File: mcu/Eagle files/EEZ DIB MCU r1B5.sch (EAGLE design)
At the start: 193 parts, among them IC1 TPD4E001DRLR, IC10 TPS61169DCKR, IC11 TPD4E001DRLR, IC12 TPA6205A1DGN, IC13 TPD4E001DRLR, IC14 TSC2007IPW, IC15 TPD4E001DRLR, IC16 DP83848CVV/NOPB, IC2 SN74LVC2G34DBVR, IC3 BTS3408G, IC4 STM32F769IGT6, IC5 LD1117ADT33TR, IC6 TPD4E001DRLR, IC7 IS42S16400J, IC8 AT24C256C-SSHL-B, IC9 TPS2051BDBVR, J1 503398-1892, J2 67803-8020, Q1 MMBT5551, SW1 TL1100CF160Q, SW2 PEC16-2215F-S0024, X1 ZL263-40DG, X2 ZL231-16KG, X3 1844249, X4 22-23-2061, X5 LMJTAB881243M-L, Y1 25MHz, Y2 XTAL016178-85SMX

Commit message: #44, #45 Eagle files
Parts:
- removed C67: 10u, EEZ_Lib1:ECAP1206
- removed C68, C69, C70, C71: 100n, rcl:C-EUC0603
- removed F1, F2: 50mA, EEZ_Lib1:FUSE_RESETTABLE21210
- removed IC14: TSC2007IPW, EEZ_Lib1:TSC2007IPW
- removed IC15: TPD4E001DRLR, EEZ_Lib1:TPD4E001-DRL
- removed IC16: DP83848CVV/NOPB, EEZ_Lib1:DP83848CVV/NOPB
- removed R50, R53, R54, R56: 2K2, rcl:R-EU_R0805
- removed R51, R52: 220R, rcl:R-EU_R0805
- removed R55: 4K87, rcl:R-EU_R0805
- removed ZD2: SMAJ18A, EEZ_Lib1:PSMAXX
- removed ZD3: BZX384-B30.115, EEZ_Lib1:ZENER-DIODESOD323
- added Q2: 2N7002, EEZ_Lib1:2N7002
- C11: value 18p -> EEEFK1V470P; device rcl:C-EUC0603 -> EEZ_Lib1:ECAPPANASONIC_H
- C12: value 4p7 -> 100n
- C13: value EEEFK1V470P -> 4u7; device EEZ_Lib1:ECAPPANASONIC_H -> EEZ_Lib1:ECAP1206
- C15: value 4u7 -> 100n; device EEZ_Lib1:ECAP1206 -> rcl:C-EUC0603
- C2, C5: value 100n -> 10n; device rcl:C-EUC0603 -> rcl:C-EUC0805
- C20: value 100n -> 4u7; device rcl:C-EUC0603 -> EEZ_Lib1:ECAP1206
- C22: value 4u7 -> 1u; device EEZ_Lib1:ECAP1206 -> rcl:C-EUC0805
- C23, C52: value 100n -> N.C.
- C24, C33, C58: value 1u -> 100n; device rcl:C-EUC0805 -> rcl:C-EUC0603
- C25: value N.C. -> 100n
- C31, C32, C46: value 100n -> 1u; device rcl:C-EUC0603 -> rcl:C-EUC0805
- C34, C48: value 1u -> 2u2
- C35: value 100n -> 2u2; device rcl:C-EUC0603 -> rcl:C-EUC0805
- C36: value 2u2 -> N.C.; device rcl:C-EUC0805 -> rcl:C-EUC0603
- C37: value 2u2 -> 4u7; device rcl:C-EUC0805 -> rcl:C-EUC1206
- C39, C53: value 4u7 -> 100n; device rcl:C-EUC1206 -> rcl:C-EUC0603
- C4: value 10n -> 100n; device rcl:C-EUC0805 -> rcl:C-EUC0603
- C45: value 100n -> 4u7; device rcl:C-EUC0603 -> rcl:C-EUC1206
- C47: device rcl:C-EUC1206 -> EEZ_Lib1:ECAP1206
- C49: value 4u7 -> N.C.; device EEZ_Lib1:ECAP1206 -> rcl:C-EUC1210
- C50: value 2u2 -> 100n; device rcl:C-EUC0805 -> rcl:C-EUC0603
- C51: value N.C. -> 4u7; device rcl:C-EUC1210 -> rcl:C-EUC1206
- C54: value 470n -> 1u
- C55: value 470n -> N.C.; device rcl:C-EUC0805 -> rcl:C-EUC0603
- C59: value N.C. -> 100n; device rcl:C-EUC0805 -> rcl:C-EUC0603
- C62: value 100n -> 10u; device rcl:C-EUC0603 -> EEZ_Lib1:ECAP1206
- C7: value 10n -> 18p; device rcl:C-EUC0805 -> rcl:C-EUC0603
- C8: value 100n -> 4p7
- IC1: value TPD4E001DRLR -> CD74HC4050PWR; device EEZ_Lib1:TPD4E001-DRL -> EEZ_DIB:CD74HC4050PWR
- IC10: value TPS61169DCKR -> TPD4E001DRLR; device EEZ_Lib1:TPS61169DCKR -> EEZ_Lib1:TPD4E001-DRL
- IC11: value TPD4E001DRLR -> TSC2007IPW; device EEZ_Lib1:TPD4E001-DRL -> EEZ_Lib1:TSC2007IPW
- IC12: value TPA6205A1DGN -> TPD4E001DRLR; device EEZ_Lib1:TPA6205 -> EEZ_Lib1:TPD4E001-DRL
- IC13: value TPD4E001DRLR -> DP83848CVV/NOPB; device EEZ_Lib1:TPD4E001-DRL -> EEZ_Lib1:DP83848CVV/NOPB
- IC2: value SN74LVC2G34DBVR -> STM32F769IGT6; device EEZ_Lib1:SN74LVC2G34DBVR -> EEZ_DIB:STM32F769IXT
- IC3: value BTS3408G -> LD1117ADT33TR; device EEZ_Lib1:BTS3408G -> v-reg:LD117ADT33TR
- IC4: value STM32F769IGT6 -> TPD4E001DRLR; device EEZ_DIB:STM32F769IXT -> EEZ_Lib1:TPD4E001-DRL
- IC5: value LD1117ADT33TR -> IS42S16400J; device v-reg:LD117ADT33TR -> EEZ_Lib1:IS42S16400
- IC6: value TPD4E001DRLR -> AT24C256C-SSHL-B; device EEZ_Lib1:TPD4E001-DRL -> EEZ_Lib1:AT24CXXSOIC8
- IC7: value IS42S16400J -> TPS2051BDBVR; device EEZ_Lib1:IS42S16400 -> EEZ_Lib1:TPS2051B
- IC8: value AT24C256C-SSHL-B -> TPS61169DCKR; device EEZ_Lib1:AT24CXXSOIC8 -> EEZ_Lib1:TPS61169DCKR
- IC9: value TPS2051BDBVR -> TPD4E001DRLR; device EEZ_Lib1:TPS2051B -> EEZ_Lib1:TPD4E001-DRL
- Q1: value MMBT5551 -> N.C.
- R18: value 10K -> N.C.
- R19, R20: value 22R -> N.C.
- R2: value 4K7 -> 10K
- R25: value 330R -> N.C.
- R28: value 47K -> N.C.
- R32: value 10K -> 1K5
- R33, R34, R37: value 10K -> 49R9
- R35, R38: value 10K -> 2K2
- R36: value 47K -> 2K2
- R39: value 1K5 -> N.C.
- R4, R8: value 1K -> 4K7
- R40, R41, R49: value 49R9 -> 2K2
- R42: value 2K2 -> 49R9
- R44: value 49R9 -> 220R
- R45: value 2K2 -> 220R
- R46: value 220R -> 2K2
- R48: value 2K2 -> 4K87
- R5: value 10K -> 1K
- R9: value 4K7 -> 1K
- SP1: value LD-BZEL-M1313 -> AI-1223-TWT or LD-BZEN 0903; device EEZ_Lib1:LD-BZEL-M1313 -> EEZ_Lib1:AI-1223-TWT-LDB0903
- SPEED: value LTST-C170YKT -> N.C.
- VBUS: value HSMG-C170 -> N.C.
- X4: value 22-23-2061 -> N.C.
- ZD1: value SMAJ18A -> BZX384-B30.115; device EEZ_Lib1:PSMAXX -> EEZ_Lib1:ZENER-DIODESOD323
- renumbered BOOT0 to BOOT1
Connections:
- removed net !AUDIO_SHDN: IC12.!SHDN, R36.1
- removed net N$166: IC12.VO-, R33.1, SP1.-
- removed net N$171: IC12.IN-, R35.1, R37.2
- removed net N$181: IC12.IN+, R32.2, R34.1
- removed net N$193: C54.1, R34.2
- removed net N$194: C59.2, IC12.BYPASS
- removed net N$195: C55.1, R35.2
- removed net N$44: F1.P$1, X3-4.1
- removed net N$45: F2.P$1, X3-5.1
- removed net N$50: IC12.VO+, R38.1, SP1.+
- removed net N$6: R37.1, R38.2
- net !FAULT: now also IC2A.PB2; no longer IC3.!FAULT, IC4A.PB2
- net !RESET: now also IC13.RESET_N, IC2C.NRST, IC4.IO3; no longer IC16.RESET_N, IC3.ENA, IC4C.NRST, IC6.IO3
- net !USB_OTG_FS_OC: now also IC2A.PD4, IC7.!OC; no longer IC4A.PD4, IC9.!OC
- net +3V3: now also C13.+, C36.1, C37.1, C38.2, C4.1, C40.1, C48.1, C52.2, C53.2, C54.2, C55.1, C65.1, C66.1, IC10.VCC, IC11.VDD/REF, IC12.VCC, IC13.IOVDD33-32, IC13.IOVDD33-48, IC1P.VDD, IC3.OUT, IC4.VCC, IC5.VDD-1, IC5.VDD-14, IC5.VDD-27, IC5.VDDQ-3, IC5.VDDQ-43, IC5.VDDQ-49, IC5.VDDQ-9, R32.2, R36.1, R39.1, R40.1, R41.1, R49.1, R6.1; no longer C15.+, C38.1, C40.2, C45.1, C46.1, C5.1, C50.1, C56.2, C57.2, C58.2, C60.1, C70.1, C71.1, IC13.VCC, IC14.VDD/REF, IC15.VCC, IC16.IOVDD33-32, IC16.IOVDD33-48, IC2P.VDD, IC5.OUT, IC7.VDD-1, IC7.VDD-14, IC7.VDD-27, IC7.VDDQ-3, IC7.VDDQ-43, IC7.VDDQ-49, IC7.VDDQ-9, IC8.VCC, R36.2, R39.2, R48.1, R50.1, R53.1, R54.1, R56.1, R9.1
- net +3V3(A): now also C57.2, C59.2, C64.1, IC13.AVDD33; no longer C62.2, C64.2, C69.1, IC16.AVDD33
- net +5V: now also C11.+, C12.1, C45.1, IC3.IN, IC7.IN; no longer C13.+, C14.1, C2.1, C47.1, C8.2, IC1.VCC, IC3.VSS, IC5.IN, IC9.IN
- net BOOT0: now also IC2C.BOOT0; no longer IC4C.BOOT0
- net BYPASS_REG: now also IC2C.BYPASS_REG; no longer IC4C.BYPASS_REG
- net DAC_OUT1: now also IC2A.PA4, Q2.G; no longer C55.2, IC4A.PA4
- net DIN2: now also IC2A.PC13, R9.2; no longer IC4A.PC13, R8.2
- net DOUT2: now also IC1C.I, IC1D.I, IC2A.PB5; no longer IC3.IN2, IC4A.PB5
- net ENC_A: now also C5.2, IC2A.PC6, R2.1; no longer C6.2, IC4A.PC6, R5.1
- net ENC_B: now also C6.1, IC2A.PC7; no longer C7.1, IC4A.PC7
- net ENC_SW: now also C2.2, IC2C.PI4; no longer C3.2, IC4C.PI4
- net EOUT_A: now also R6.2; no longer R9.2
- net EOUT_B: now also R2.2; no longer R5.2
- net ETH_COL: now also IC2A.PA3; no longer IC4A.PA3
- net ETH_CRS: now also IC2A.PA0; no longer IC4A.PA0
- net ETH_MDC: now also IC13.MDC, IC2A.PC1; no longer IC16.MDC, IC4A.PC1
- net ETH_MDIO: now also IC13.MDIO, IC2A.PA2, R32.1; no longer IC16.MDIO, IC4A.PA2, R39.1
- net ETH_RXD0: now also IC2A.PC4; no longer IC4A.PC4
- net ETH_RXD1: now also IC2A.PC5; no longer IC4A.PC5
- net ETH_RXD2: now also IC2B.PH6; no longer IC4B.PH6
- net ETH_RXD3: now also IC2B.PH7; no longer IC4B.PH7
- net ETH_RX_CLK: now also IC2A.PA1; no longer IC4A.PA1
- net ETH_RX_DV: now also IC2A.PA7; no longer IC4A.PA7
- net ETH_RX_ERR: now also IC2A.PB10; no longer IC4A.PB10
- net ETH_TXD0: now also IC2A.PB12; no longer IC4A.PB12
- net ETH_TXD1: now also IC2A.PB13; no longer IC4A.PB13
- net ETH_TXD2: now also IC2A.PC2; no longer IC4A.PC2
- net ETH_TXD3: now also IC2A.PB8; no longer IC4A.PB8
- net ETH_TX_CLK: now also IC2A.PC3; no longer IC4A.PC3
- net ETH_TX_EN: now also IC2A.PB11; no longer IC4A.PB11
- net FMC_A0: now also IC2B.PF0, IC5.A0; no longer IC4B.PF0, IC7.A0
- net FMC_A1: now also IC2B.PF1, IC5.A1; no longer IC4B.PF1, IC7.A1
- net FMC_A10: now also IC2B.PG0, IC5.A10/AP; no longer IC4B.PG0, IC7.A10/AP
- net FMC_A11: now also IC2B.PG1, IC5.A11; no longer IC4B.PG1, IC7.A11
- net FMC_A2: now also IC2B.PF2, IC5.A2; no longer IC4B.PF2, IC7.A2
- net FMC_A3: now also IC2B.PF3, IC5.A3; no longer IC4B.PF3, IC7.A3
- net FMC_A4: now also IC2B.PF4, IC5.A4; no longer IC4B.PF4, IC7.A4
- net FMC_A5: now also IC2B.PF5, IC5.A5; no longer IC4B.PF5, IC7.A5
- net FMC_A6: now also IC2B.PF12, IC5.A6; no longer IC4B.PF12, IC7.A6
- net FMC_A7: now also IC2B.PF13, IC5.A7; no longer IC4B.PF13, IC7.A7
- net FMC_A8: now also IC2B.PF14, IC5.A8; no longer IC4B.PF14, IC7.A8
- net FMC_A9: now also IC2B.PF15, IC5.A9; no longer IC4B.PF15, IC7.A9
- net FMC_BA0: now also IC2B.PG4, IC5.BA0; no longer IC4B.PG4, IC7.BA0
- net FMC_BA1: now also IC2B.PG5, IC5.BA1; no longer IC4B.PG5, IC7.BA1
- net FMC_D0: now also IC2A.PD14, IC5.DQ0; no longer IC4A.PD14, IC7.DQ0
- net FMC_D1: now also IC2A.PD15, IC5.DQ1; no longer IC4A.PD15, IC7.DQ1
- net FMC_D10: now also IC2B.PE13, IC5.DQ10; no longer IC4B.PE13, IC7.DQ10
- net FMC_D11: now also IC2B.PE14, IC5.DQ11; no longer IC4B.PE14, IC7.DQ11
- net FMC_D12: now also IC2B.PE15, IC5.DQ12; no longer IC4B.PE15, IC7.DQ12
- net FMC_D13: now also IC2A.PD8, IC5.DQ13; no longer IC4A.PD8, IC7.DQ13
- net FMC_D14: now also IC2A.PD9, IC5.DQ14; no longer IC4A.PD9, IC7.DQ14
- net FMC_D15: now also IC2A.PD10, IC5.DQ15; no longer IC4A.PD10, IC7.DQ15
- net FMC_D2: now also IC2A.PD0, IC5.DQ2; no longer IC4A.PD0, IC7.DQ2
- net FMC_D3: now also IC2A.PD1, IC5.DQ3; no longer IC4A.PD1, IC7.DQ3
- net FMC_D4: now also IC2B.PE7, IC5.DQ4; no longer IC4B.PE7, IC7.DQ4
- net FMC_D5: now also IC2B.PE8, IC5.DQ5; no longer IC4B.PE8, IC7.DQ5
- net FMC_D6: now also IC2B.PE9, IC5.DQ6; no longer IC4B.PE9, IC7.DQ6
- net FMC_D7: now also IC2B.PE10, IC5.DQ7; no longer IC4B.PE10, IC7.DQ7
- net FMC_D8: now also IC2B.PE11, IC5.DQ8; no longer IC4B.PE11, IC7.DQ8
- net FMC_D9: now also IC2B.PE12, IC5.DQ9; no longer IC4B.PE12, IC7.DQ9
- net FMC_NBL0: now also IC2B.PE0, IC5.LDQM; no longer IC4B.PE0, IC7.LDQM
- net FMC_NBL1: now also IC2B.PE1, IC5.UDQM; no longer IC4B.PE1, IC7.UDQM
- net FMC_SDCKE0: now also IC2B.PH2, IC5.CKE; no longer IC4B.PH2, IC7.CKE
- net FMC_SDCLK: now also IC2B.PG8, IC5.CLK; no longer IC4B.PG8, IC7.CLK
- net FMC_SDNCAS: now also IC2B.PG15, IC5.!CAS; no longer IC4B.PG15, IC7.!CAS
- net FMC_SDNE0: now also IC2B.PH3, IC5.!CS; no longer IC4B.PH3, IC7.!CS
- net FMC_SDNRAS: now also IC2B.PF11, IC5.!RAS; no longer IC4B.PF11, IC7.!RAS
- net FMC_SDNWE: now also IC2B.PH5, IC5.!WE; no longer IC4B.PH5, IC7.!WE
- net GND: now also C11.-, C15.2, C2.1, C20.-, C22.2, C38.1, C4.2, C40.2, C47.-, C49.2, C5.1, C50.1, C51.1, C54.1, C55.2, C56.2, C58.2, C6.2, C62.-, C64.2, C7.1, C8.2, IC11.A0, IC11.A1, IC13.AGND-15, IC13.AGND-19, IC13.DGND, IC13.IOGND-35, IC13.IOGND-47, IC1P.VSS, IC2D.VSS, IC2D.VSSA, IC2D.VSSDSI, IC2D.VSSDSI_2, IC2D.VSS_10, IC2D.VSS_2, IC2D.VSS_3, IC2D.VSS_4, IC2D.VSS_5, IC2D.VSS_6, IC2D.VSS_7, IC2D.VSS_8, IC2D.VSS_9, IC3.ADJ, IC4.GND, IC5.GND, IC5.GND-28, IC5.GND-54, IC5.GNDQ-12, IC5.GNDQ-46, IC5.GNDQ-52, IC5.GNDQ-6, IC6.A0, IC6.A1, IC6.A2, IC6.WP, Q2.S, R35.1, R38.1, R48.1; no longer C11.1, C15.-, C2.2, C20.2, C22.-, C38.2, C4.1, C40.1, C47.2, C49.-, C5.2, C50.2, C51.2, C54.2, C56.1, C58.1, C6.1, C62.1, C64.1, C67.-, C68.2, C69.2, C7.2, C70.2, C71.2, C8.1, IC1.GND, IC12.TP, IC13.GND, IC14.A0, IC14.A1, IC14.GND, IC15.GND, IC16.AGND-15, IC16.AGND-19, IC16.DGND, IC16.IOGND-35, IC16.IOGND-47, IC2P.VSS, IC3.GND, IC4D.VSS, IC4D.VSSA, IC4D.VSSDSI, IC4D.VSSDSI_2, IC4D.VSS_10, IC4D.VSS_2, IC4D.VSS_3, IC4D.VSS_4, IC4D.VSS_5, IC4D.VSS_6, IC4D.VSS_7, IC4D.VSS_8, IC4D.VSS_9, IC5.ADJ, IC7.GND-28, IC7.GND-54, IC7.GNDQ-12, IC7.GNDQ-46, IC7.GNDQ-52, IC7.GNDQ-6, IC8.A0, IC8.A1, IC8.A2, IC8.WP, R42.1, R45.1, R55.1, ZD1.A, ZD2.A
- net I2C1_SCL: now also IC11.SCL, IC2A.PB6, IC6.SCL; no longer IC14.SCL, IC4A.PB6, IC8.SCL
- net I2C1_SDA: now also IC11.SDA, IC2A.PB7, IC6.SDA; no longer IC14.SDA, IC4A.PB7, IC8.SDA
- net IRQ_TOUCH: now also IC11.!PENIRQ, IC2A.PD7; no longer IC14.!PENIRQ, IC4A.PD7
- net LED_ACT: now also IC13.AN_EN(LED_ACT/COL), R36.2, R44.2; no longer IC16.AN_EN(LED_ACT/COL), R43.2, R51.2
- net LED_LINK: now also IC13.AN_0(LED_LINK), R43.2, R45.2; no longer IC16.AN_0(LED_LINK), R50.2, R52.2
- net LED_SPEED: now also IC13.AN_1(LED_SPEED), R41.2; no longer IC16.AN_1(LED_SPEED), R48.2
- net LTDC_B2: now also IC2A.PD6; no longer IC4A.PD6
- net LTDC_B3: now also IC2B.PG11; no longer IC4B.PG11
- net LTDC_B4: now also IC2B.PG12; no longer IC4B.PG12
- net LTDC_B5: now also IC2C.PI5; no longer IC4C.PI5
- net LTDC_B6: now also IC2C.PI6; no longer IC4C.PI6
- net LTDC_B7: now also IC2C.PI7; no longer IC4C.PI7
- net LTDC_CLK: now also IC2B.PG7; no longer IC4B.PG7
- net LTDC_DE: now also IC2B.PF10; no longer IC4B.PF10
- net LTDC_G2: now also IC2A.PA6; no longer IC4A.PA6
- net LTDC_G3: now also IC2B.PG10; no longer IC4B.PG10
- net LTDC_G4: now also IC2B.PH4; no longer IC4B.PH4
- net LTDC_G5: now also IC2C.PI0; no longer IC4C.PI0
- net LTDC_G6: now also IC2C.PI11; no longer IC4C.PI11
- net LTDC_G7: now also IC2A.PD3; no longer IC4A.PD3
- net LTDC_HSYNC: now also IC2C.PI10; no longer IC4C.PI10
- net LTDC_R2: now also IC2A.PC10; no longer IC4A.PC10
- net LTDC_R3: now also IC2A.PB0; no longer IC4A.PB0
- net LTDC_R4: now also IC2A.PA5; no longer IC4A.PA5
- net LTDC_R5: now also IC2A.PC0; no longer IC4A.PC0
- net LTDC_R6: now also IC2A.PB1; no longer IC4A.PB1
- net LTDC_R7: now also IC2B.PG6; no longer IC4B.PG6
- net LTDC_VSYNC: now also IC2C.PI9; no longer IC4C.PI9
- net MCLK_25: now also IC2A.PC9; no longer IC4A.PC9
- net N$1: now also IC13.TX_CLK; no longer IC16.TX_CLK
- net N$10: now also IC13.TX_EN; no longer IC16.TX_EN
- net N$101: now also R39.2; no longer R46.2
- net N$102: now also C58.1, R37.1, R42.2; no longer C63.1, R44.1, R49.2
- net N$11: now also IC13.MII_MODE(RX_DV); no longer IC16.MII_MODE(RX_DV)
- net N$12: now also IC13.RX_CLK; no longer IC16.RX_CLK
- net N$15: now also IC13.TXD_0; no longer IC16.TXD_0
- net N$17: now also IC13.TXD_1; no longer IC16.TXD_1
- net N$178: now also IC2D.VCAPDSI, IC2D.VDD12DSI; no longer IC4D.VCAPDSI, IC4D.VDD12DSI
- net N$21: now also IC13.TXD_2; no longer IC16.TXD_2
- net N$22: now also IC13.X1; no longer IC16.X1
- net N$23: now also R40.2; no longer R47.2
- net N$25: now also R38.2; no longer R45.2
- net N$26: now also R35.2; no longer R42.2
- net N$27: now also IC13.PWR_DOWN/INT; no longer IC16.PWR_DOWN/INT
- net N$28: now also R49.2; no longer R56.2
- net N$29: now also IC13.TXD_3/SNI_MODE; no longer IC16.TXD_3/SNI_MODE
- net N$3: now also C56.1, R33.1, R34.2; no longer C61.1, R40.1, R41.2
- net N$30: now also IC8.VIN; no longer IC10.VIN
- net N$31: now also IC13.PHYAD4(RXD1_3); no longer IC16.PHYAD4(RXD1_3)
- net N$32: now also IC13.PHYAD3(RXD1_2); no longer IC16.PHYAD3(RXD1_2)
- net N$33: now also IC13.PHYAD0(COL); no longer IC16.PHYAD0(COL)
- net N$34: now also IC13.PHYAD2(RXD1_1); no longer IC16.PHYAD2(RXD1_1)
- net N$35: now also IC13.PHYAD1(RXD1_0); no longer IC16.PHYAD1(RXD1_0)
- net N$36: now also IC13.MDIX_EN(RX_ER); no longer IC16.MDIX_EN(RX_ER)
- net N$37: now also IC13.CRS/CRS_DV/LED_CFG; no longer IC16.CRS/CRS_DV/LED_CFG
- net N$38: now also R3.2, R4.1; no longer R2.2, R3.1
- net N$39: now also R3.1; no longer R2.1
- net N$40: now also R7.1; no longer R6.1
- net N$41: now also R7.2, R8.1; no longer R6.2, R7.1
- net N$42: now also IC1F.O, R5.1; no longer IC2A.O, R4.1
- net N$43: now also IC1A.O, R9.1; no longer IC2B.O, R8.1
- net N$46: now also IC1F.I, R4.2; no longer IC1.IO1, IC2A.I, R3.2
- net N$47: now also IC1A.I, R8.2; no longer IC1.IO2, IC2B.I, R7.2
- net N$48: now also IC1B.O, IC1E.O, X3-4.1; no longer F1.P$2, IC1.IO3, IC3.OUT1, ZD1.C
- net N$49: now also IC1C.O, IC1D.O, X3-5.1; no longer F2.P$2, IC1.IO4, IC3.OUT2, ZD2.C
- net N$5: now also Q2.D, SP1.-; no longer R32.1, R33.2
- net N$52: now also C51.2, SP1.+; no longer C53.2, IC12.VDD
- net N$8: now also R44.1; no longer R51.1
- net N$9: now also R45.1; no longer R52.1
- net N$97: now also IC13.RBIAS, R48.2; no longer IC16.RBIAS, R55.2
- net N$98: now also IC13.RESERVED-21, R46.2; no longer IC16.RESERVED-21, R53.2
- net N$99: now also IC13.RESERVED-20, R47.2; no longer IC16.RESERVED-20, R54.2
- net OE_SYNC: now also IC2A.PD13; no longer IC4A.PD13
- net PE: now also C49.1; no longer C51.1
- net PFBOUT: now also C60.1, C61.1, C62.+, C63.1, IC13.PFBIN1, IC13.PFBIN2, IC13.PFBOUT; no longer C65.1, C66.1, C67.+, C68.1, IC16.PFBIN1, IC16.PFBIN2, IC16.PFBOUT
- net PWR_DIRECT: now also IC2B.PG2; no longer IC4B.PG2
- net PWR_SSTART: now also IC2B.PG3; no longer IC4B.PG3
- net RCC_OSC32_IN: now also C8.1, IC2A.PC14; no longer C10.1, IC4A.PC14
- net RCC_OSC32_OUT: now also C10.1, IC2A.PC15; no longer C12.1, IC4A.PC15
- net RCC_OSC_IN: now also C7.2, IC2B.PH0; no longer C9.2, IC4B.PH0
- net RCC_OSC_OUT: now also C9.2, IC2B.PH1; no longer C11.2, IC4B.PH1
- net RD+: now also IC12.IO3, IC13.RD+, R37.2; no longer IC15.IO3, IC16.RD+, R44.2
- net RD-: now also IC12.IO4, IC13.RD-, R42.1; no longer IC15.IO4, IC16.RD-, R49.1
- net SDMMC1_CK: now also IC2A.PC12; no longer IC4A.PC12
- net SDMMC1_CMD: now also IC2A.PD2; no longer IC4A.PD2
- net SDMMC1_D0: now also IC2A.PC8; no longer IC4A.PC8
- net SD_DETECT: now also IC2A.PC11; no longer IC4A.PC11
- net SPI2_CLK: now also IC2C.PI1; no longer IC4C.PI1
- net SPI2_CSA: now also IC2A.PD12; no longer IC4A.PD12
- net SPI2_CSB: now also IC2A.PD11; no longer IC4A.PD11
- net SPI2_IRQ: now also IC2A.PA8; no longer IC4A.PA8
- net SPI2_MISO: now also IC2A.PB14; no longer IC4A.PB14
- net SPI2_MOSI: now also IC2C.PI3; no longer IC4C.PI3
- net SPI4_CLK: now also IC2B.PE2; no longer IC4B.PE2
- net SPI4_CSA: now also IC2B.PE3; no longer IC4B.PE3
- net SPI4_CSB: now also IC2B.PE4; no longer IC4B.PE4
- net SPI4_IRQ: now also IC2A.PB9; no longer IC4A.PB9
- net SPI4_MISO: now also IC2B.PE5; no longer IC4B.PE5
- net SPI4_MOSI: now also IC2B.PE6; no longer IC4B.PE6
- net SPI5_CLK: now also IC2B.PF7; no longer IC4B.PF7
- net SPI5_CSA: now also IC2B.PG14; no longer IC4B.PG14
- net SPI5_CSB: now also IC2B.PG13; no longer IC4B.PG13
- net SPI5_IRQ: now also IC2A.PA15; no longer IC4A.PA15
- net SPI5_MISO: now also IC2B.PF8; no longer IC4B.PF8
- net SPI5_MOSI: now also IC2B.PF9; no longer IC4B.PF9
- net SW_WLED: now also IC8.SW; no longer IC10.SW
- net SYS_JTCK-SWCLK: now also IC2A.PA14; no longer IC4A.PA14
- net SYS_JTDO-SWO: now also IC2A.PB3, IC4.IO4; no longer IC4A.PB3, IC6.IO4
- net SYS_JTMS-SWDIO: now also IC2A.PA13; no longer IC4A.PA13
- net TCK: now also IC4.IO1; no longer IC6.IO1
- net TD+: now also IC12.IO1, IC13.TD+, R33.2; no longer IC15.IO1, IC16.TD+, R40.2
- net TD-: now also IC12.IO2, IC13.TD-, R34.1; no longer IC15.IO2, IC16.TD-, R41.1
- net TFT_BRIGHTNESS: now also IC2A.PB15, IC8.CTRL; no longer IC10.CTRL, IC4A.PB15
- net TMS: now also IC4.IO2; no longer IC6.IO2
- net UART_RX/DIN1: now also IC2B.PF6, R5.2; no longer IC4B.PF6, R4.2
- net UART_TX/DOUT1: now also IC1B.I, IC1E.I, IC2A.PB4; no longer IC3.IN1, IC4A.PB4
- net USB_D_N: now also IC9.IO1; no longer IC11.IO1
- net USB_D_P: now also IC9.IO2; no longer IC11.IO2
- net USB_OTG_FS_D_N: now also IC2A.PA11; no longer IC4A.PA11
- net USB_OTG_FS_D_P: now also IC2A.PA12; no longer IC4A.PA12
- net USB_OTG_FS_ID: now also IC2A.PA10, IC9.IO3; no longer IC11.IO3, IC4A.PA10
- net USB_OTG_FS_PSO: now also IC2A.PD5, IC7.EN; no longer IC4A.PD5, IC9.EN
- net USB_OTG_FS_VBUS: now also C47.+, C50.2, IC2A.PA9, IC7.OUT, IC9.VCC; no longer C49.+, C52.2, IC11.VCC, IC4A.PA9, IC9.OUT
- net USER_SW: now also C3.2, IC2B.PG9; no longer C4.2, IC4B.PG9
- net VBAT: now also IC2D.VBAT; no longer IC4D.VBAT
- net VCAP1: now also C35.1, IC2D.VCAP_1; no longer C37.1, IC4D.VCAP_1
- net VCAP2: now also C34.1, IC2D.VCAP_2; no longer C36.1, IC4D.VCAP_2
- net VDD: now also C14.1, C15.1, C20.+, C22.1, IC2C.PDR_ON, IC2D.VDD, IC2D.VDDDSI, IC2D.VDDSDMMC, IC2D.VDDUSB, IC2D.VDD_10, IC2D.VDD_11, IC2D.VDD_12, IC2D.VDD_2, IC2D.VDD_3, IC2D.VDD_4, IC2D.VDD_5, IC2D.VDD_6, IC2D.VDD_7, IC2D.VDD_8, IC2D.VDD_9; no longer C20.1, C22.+, C32.1, C33.1, IC4C.PDR_ON, IC4D.VDD, IC4D.VDDDSI, IC4D.VDDSDMMC, IC4D.VDDUSB, IC4D.VDD_10, IC4D.VDD_11, IC4D.VDD_12, IC4D.VDD_2, IC4D.VDD_3, IC4D.VDD_4, IC4D.VDD_5, IC4D.VDD_6, IC4D.VDD_7, IC4D.VDD_8, IC4D.VDD_9
- net VDDA: now also C32.1, C33.1, IC2D.VDDA; no longer C34.1, C35.1, IC4D.VDDA
- net VLED+: now also C46.1, ZD1.C; no longer C48.1, ZD3.C
- net VLED-: now also IC8.FB, ZD1.A; no longer IC10.FB, ZD3.A
- net VREF+: now also IC2D.VREF+; no longer IC4D.VREF+
- net XL: now also IC10.IO3, IC11.X-; no longer IC13.IO3, IC14.X-
- net XR: now also IC10.IO1, IC11.X+; no longer IC13.IO1, IC14.X+
- net YD: now also IC10.IO2, IC11.Y-; no longer IC13.IO2, IC14.Y-
- net YU: now also IC10.IO4, IC11.Y+; no longer IC13.IO4, IC14.Y+
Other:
- note added: "Audio output"
- note added: "JTAG/SWD (optional)"
- note removed: "Audio amplifier"
- note removed: "Consumption: +3.3 V, max. 220 mA"
- note removed: "JTAG (SWD)"
- moved on the sheet: C10, C12, C13, C14, C16, C17, C18, C19, C2, C21, C23, C24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

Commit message: #46
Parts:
- removed JP2, JP3: JP2-CUT, EEZ_Lib1:JP2-CUT
- added SCL, SDA: JP2-NOCUT, EEZ_Lib1:JP2-NOCUT
- C1, C49: device rcl:C-EUC1210 -> rcl:C-EUC0805
- X2: device EEZ_connectors:IDC-16PIN-ANGLED -> EEZ_connectors:IDC-16PIN
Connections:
- net I2C1_SCL: now also SCL.1; no longer JP2.1
- net I2C1_SDA: now also SDA.2; no longer JP3.2
- net N$13: now also SDA.1; no longer JP3.1
- net N$7: now also SCL.2; no longer JP2.2
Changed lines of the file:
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@@
 <part name="PE3" library="supply1" deviceset="PE" device=""/>
 <part name="X1" library="EEZ_connectors" deviceset="ZL263-40DG" device="" value="ZL263-40DG"/>
-<part name="X2" library="EEZ_connectors" deviceset="IDC-16PIN" device="-ANGLED" value="ZL231-16KG"/>
+<part name="X2" library="EEZ_connectors" deviceset="IDC-16PIN" device="" value="ZL231-16KG"/>
 <part name="X3" library="EEZ_connectors" deviceset="MC1,5/5-G-3,5" device="" value="1844249"/>
 <part name="SUPPLY48" library="supply2" deviceset="GND" device=""/>
@@
 <part name="JP8" library="EEZ_Lib1" deviceset="JP3-CUT" device=""/>
 <part name="+3V17" library="supply1" deviceset="+3V3" device=""/>
-<part name="C1" library="rcl" deviceset="C-EU" device="C1210" value="N.C."/>
+<part name="C1" library="rcl" deviceset="C-EU" device="C0805" value="N.C."/>
 <part name="SUPPLY19" library="supply2" deviceset="GND" device=""/>
-<part name="C49" library="rcl" deviceset="C-EU" device="C1210" value="N.C."/>
+<part name="C49" library="rcl" deviceset="C-EU" device="C0805" value="N.C."/>
 <part name="Y2" library="EEZ_Lib1" deviceset="XTAL" device="85SMX" value="XTAL016178-85SMX"/>
 <part name="C8" library="rcl" deviceset="C-EU" device="C0603" value="4p7"/>
@@
 <part name="SUPPLY16" library="supply2" deviceset="GND" device=""/>
 <part name="JP5" library="EEZ_Lib1" deviceset="JP2-CUT" device=""/>
-<part name="JP2" library="EEZ_Lib1" deviceset="JP2-CUT" device=""/>
-<part name="JP3" library="EEZ_Lib1" deviceset="JP2-CUT" device=""/>
+<part name="SCL" library="EEZ_Lib1" deviceset="JP2-NOCUT" device=""/>
+<part name="SDA" library="EEZ_Lib1" deviceset="JP2-NOCUT" device=""/>
 <part name="BOOT1" library="EEZ_Lib1" deviceset="JUMPER-2PIN" device="-2MM"/>
 <part name="+3V18" library="supply1" deviceset="+3V3" device=""/>
@@
 <attribute name="NAME" x="19.685" y="168.91" size="1.778" layer="95"/>
 </instance>
-<instance part="JP2" gate="G$1" x="22.86" y="139.7" smashed="yes">
+<instance part="SCL" gate="G$1" x="22.86" y="139.7" smashed="yes">
 <attribute name="NAME" x="22.86" y="140.335" size="1.27" layer="95"/>
 </instance>
-<instance part="JP3" gate="G$1" x="66.04" y="139.7" smashed="yes">
+<instance part="SDA" gate="G$1" x="66.04" y="139.7" smashed="yes">
 <attribute name="NAME" x="65.405" y="140.335" size="1.27" layer="95"/>
 </instance>
@@
 <segment>
 <label x="78.74" y="140.335" size="1.27" layer="102" rot="MR0"/>
-<pinref part="JP3" gate="G$1" pin="2"/>
+<pinref part="SDA" gate="G$1" pin="2"/>
 <wire x1="68.58" y1="139.7" x2="78.74" y2="139.7" width="0.1524" layer="91"/>
 </segment>
@@
 <segment>
 <label x="12.7" y="140.335" size="1.27" layer="102"/>
-<pinref part="JP2" gate="G$1" pin="1"/>
+<pinref part="SCL" gate="G$1" pin="1"/>
 <wire x1="22.86" y1="139.7" x2="12.7" y2="139.7" width="0.1524" layer="91"/>
 </segment>
@@
 <net name="N$7" class="0">
 <segment>
-<pinref part="JP2" gate="G$1" pin="2"/>
+<pinref part="SCL" gate="G$1" pin="2"/>
 <pinref part="X2" gate="-13" pin="1"/>
 <wire x1="25.4" y1="139.7" x2="30.48" y2="139.7" width="0.1524" layer="91"/>
@@
 <segment>
 <pinref part="X2" gate="-14" pin="1"/>
-<pinref part="JP3" gate="G$1" pin="1"/>
+<pinref part="SDA" gate="G$1" pin="1"/>
 <wire x1="60.96" y1="139.7" x2="66.04" y2="139.7" width="0.1524" layer="91"/>
 </segment>

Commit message: MCU board BOM update
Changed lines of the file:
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@@
 <setting verticaltext="up"/>
 </settings>
-<grid distance="0.1" unitdist="inch" unit="inch" style="lines" multiple="1" display="no" altdistance="0.01" altunitdist="inch" altunit="inch"/>
+<grid distance="0.025" unitdist="inch" unit="inch" style="lines" multiple="4" display="no" altdistance="0.01" altunitdist="inch" altunit="inch"/>
 <layers>
 <layer number="1" name="Top" color="4" fill="1" visible="no" active="no"/>
@@
 <text x="165.1" y="27.94" size="2.54" layer="94" font="vector">STM32F7 MCU</text>
 <text x="233.68" y="63.5" size="1.27" layer="103">Tant.</text>
+<rectangle x1="254.635" y1="149.86" x2="259.715" y2="157.48" layer="97"/>
 </plain>
 <instances>

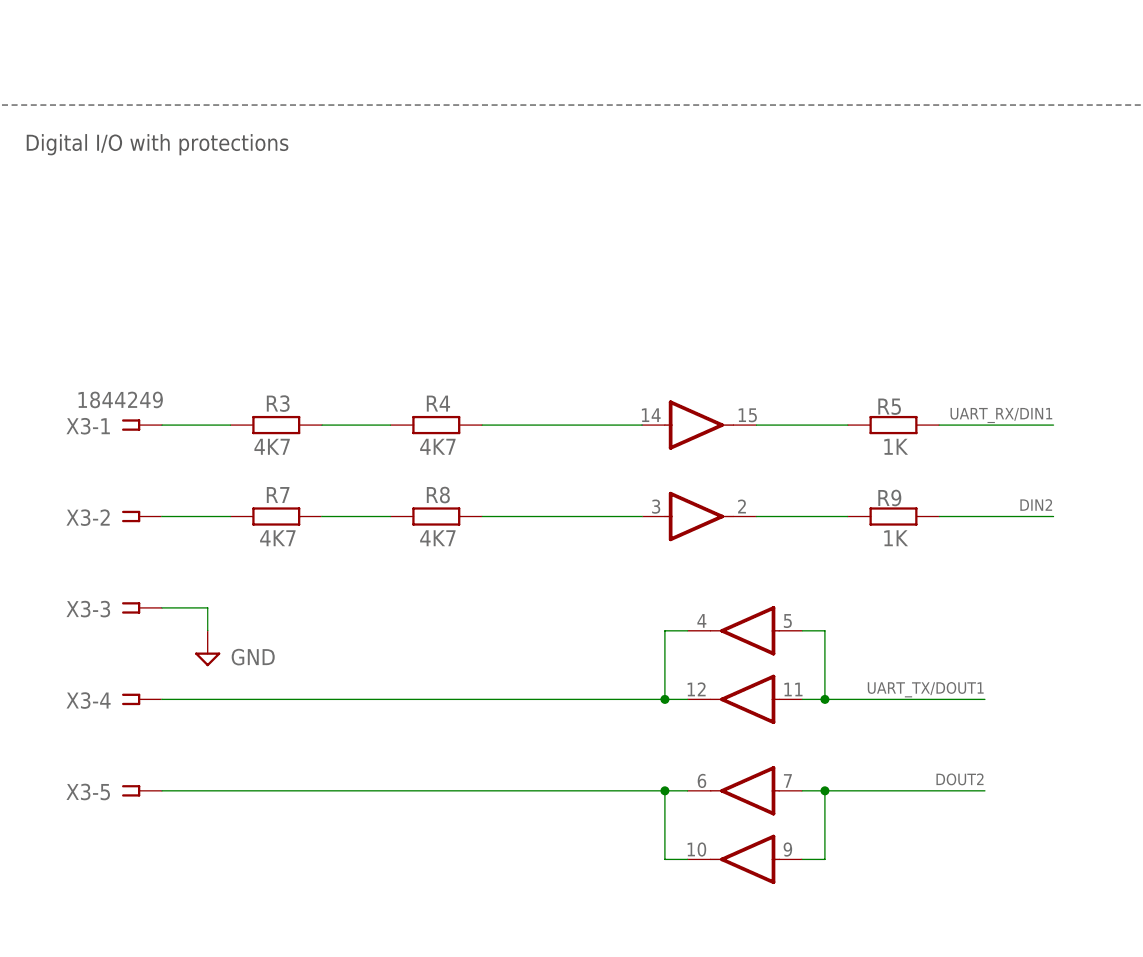
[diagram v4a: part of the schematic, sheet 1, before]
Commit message: MCU optional I/O protection
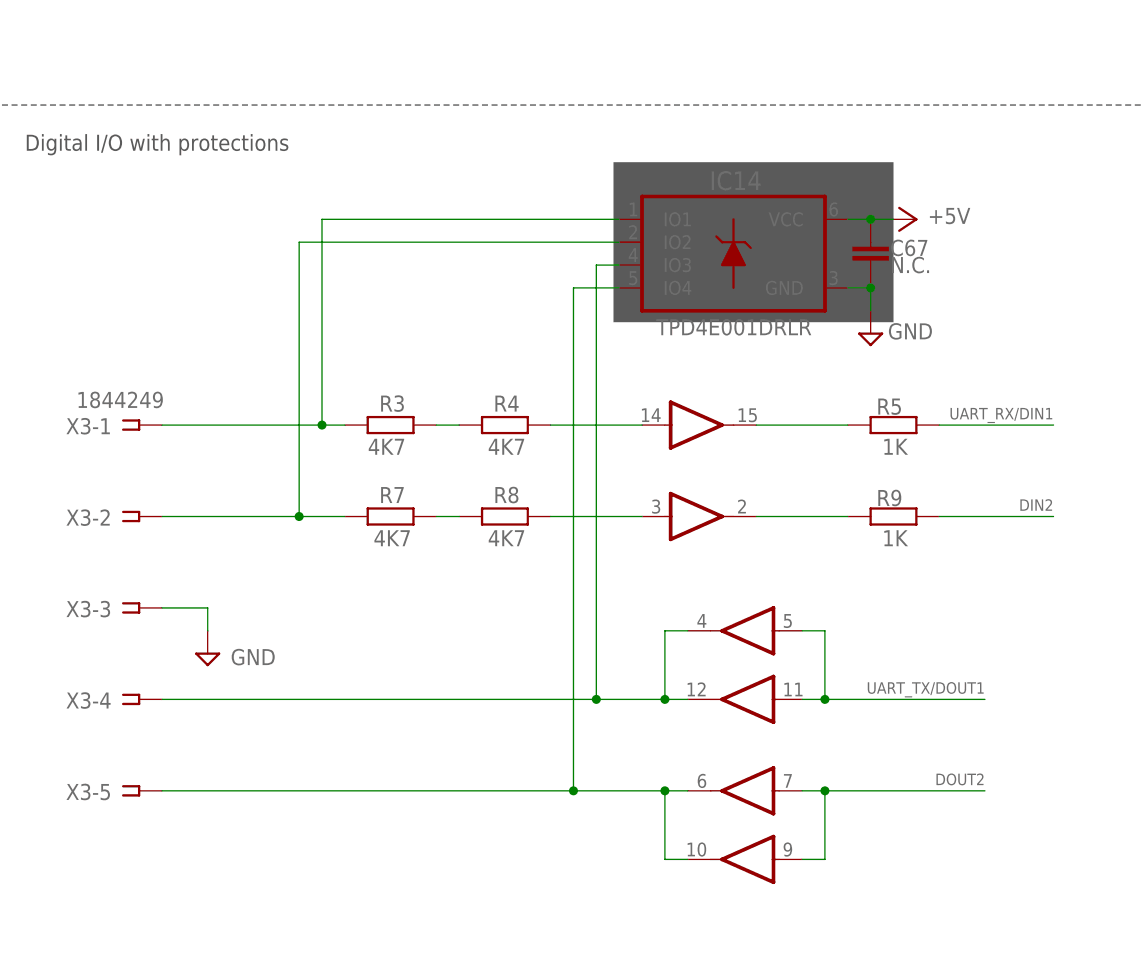
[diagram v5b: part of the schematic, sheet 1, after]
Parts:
- added C67: N.C., rcl:C-EUC0603
- added IC14: TPD4E001DRLR, EEZ_Lib1:TPD4E001-DRL
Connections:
- removed net N$39: R3.1, X3-1.1
- removed net N$40: R7.1, X3-2.1
- new net N$14: IC14.IO2, R7.1, X3-2.1
- new net N$6: IC14.IO1, R3.1, X3-1.1
- net +5V: now also C67.1, IC14.VCC
- net GND: now also C67.2, IC14.GND
- net N$48: now also IC14.IO3
- net N$49: now also IC14.IO4
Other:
- moved on the sheet: R3, R4, R7, R8

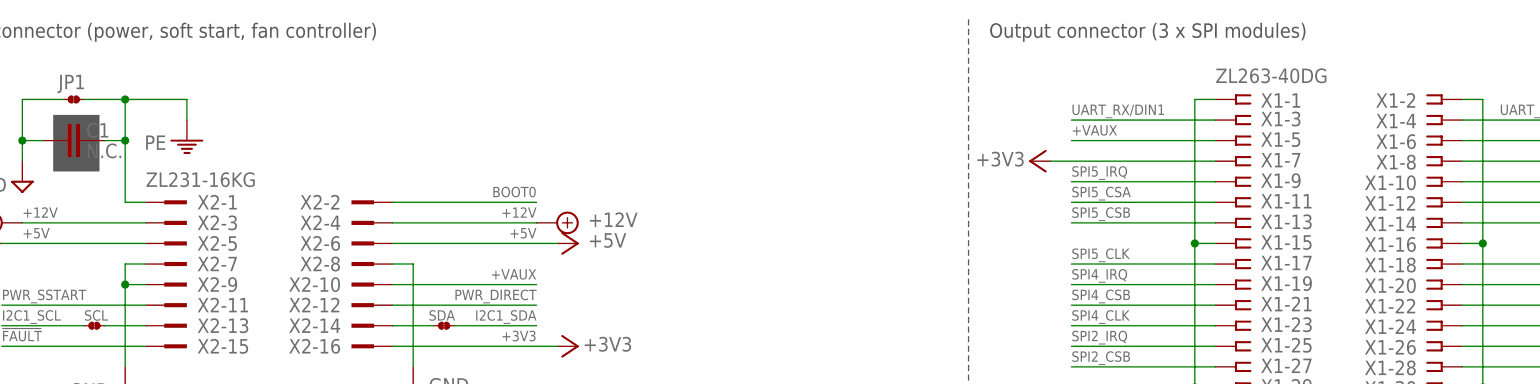
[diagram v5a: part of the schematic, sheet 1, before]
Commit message: update TME connectors in BOMs
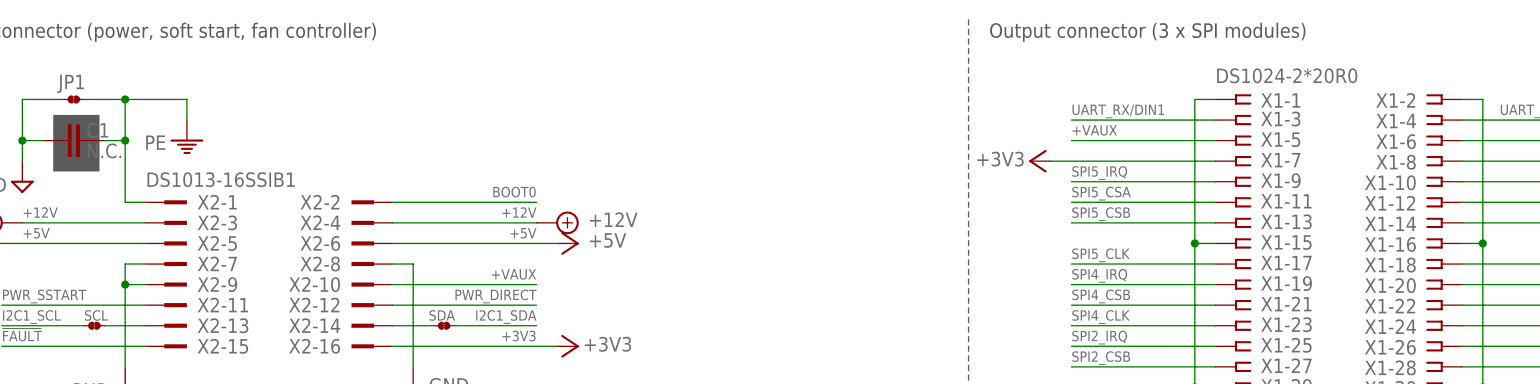
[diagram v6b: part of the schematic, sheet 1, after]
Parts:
- X1: value ZL263-40DG -> DS1024-2*20R0
- X2: value ZL231-16KG -> DS1013-16SSIB1
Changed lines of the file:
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@@
 <setting verticaltext="up"/>
 </settings>
-<grid distance="0.1" unitdist="inch" unit="inch" style="lines" multiple="1" display="no" altdistance="0.01" altunitdist="inch" altunit="inch"/>
+<grid distance="0.025" unitdist="inch" unit="inch" style="lines" multiple="4" display="no" altdistance="0.01" altunitdist="inch" altunit="inch"/>
 <layers>
 <layer number="1" name="Top" color="4" fill="1" visible="no" active="no"/>
@@
 <part name="SUPPLY3" library="supply2" deviceset="GND" device=""/>
 <part name="PE3" library="supply1" deviceset="PE" device=""/>
-<part name="X1" library="EEZ_connectors" deviceset="ZL263-40DG" device="" value="ZL263-40DG"/>
-<part name="X2" library="EEZ_connectors" deviceset="IDC-16PIN" device="" value="ZL231-16KG"/>
+<part name="X1" library="EEZ_connectors" deviceset="ZL263-40DG" device="" value="DS1024-2*20R0"/>
+<part name="X2" library="EEZ_connectors" deviceset="IDC-16PIN" device="" value="DS1013-16SSIB1"/>
 <part name="X3" library="EEZ_connectors" deviceset="MC1,5/5-G-3,5" device="" value="1844249"/>
 <part name="SUPPLY48" library="supply2" deviceset="GND" device=""/>
